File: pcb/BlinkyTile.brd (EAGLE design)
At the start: 49.8 x 47.4 mm, 9 parts

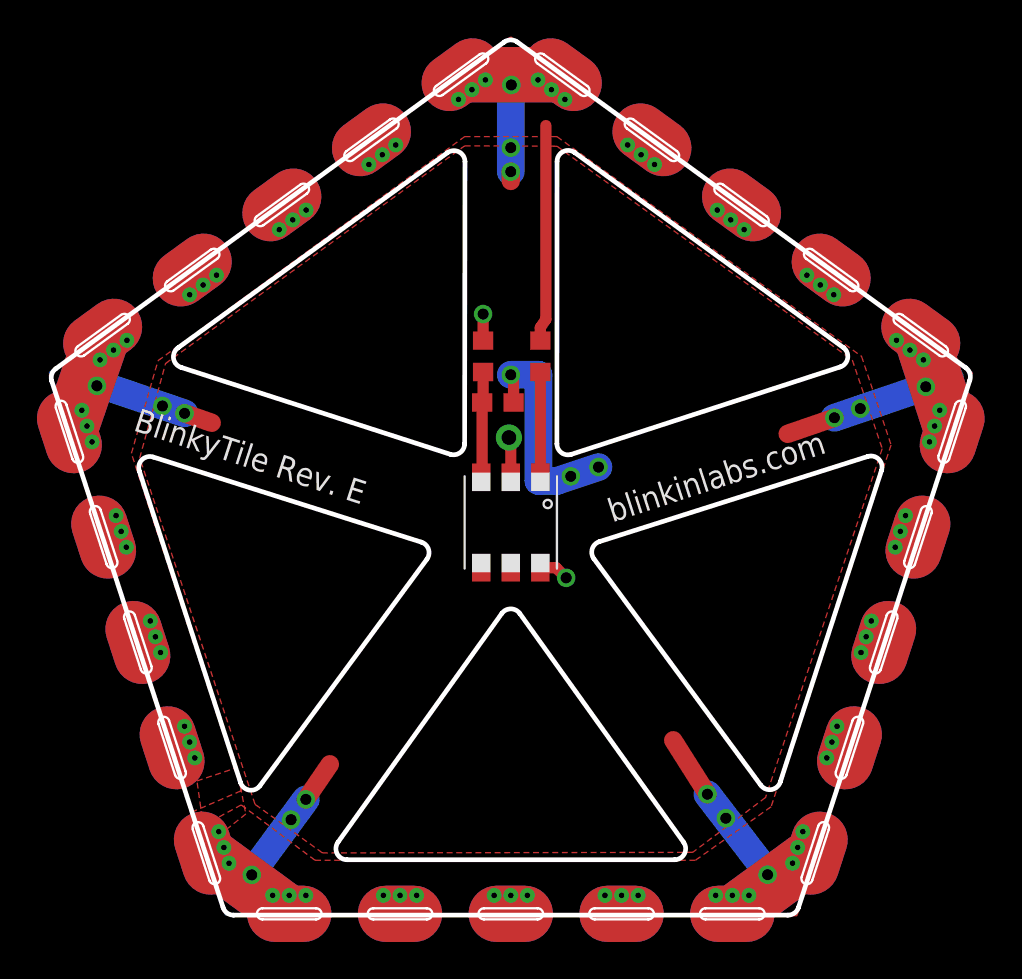
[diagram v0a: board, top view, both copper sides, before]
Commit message: Put address line on edge, tighten R and C positions
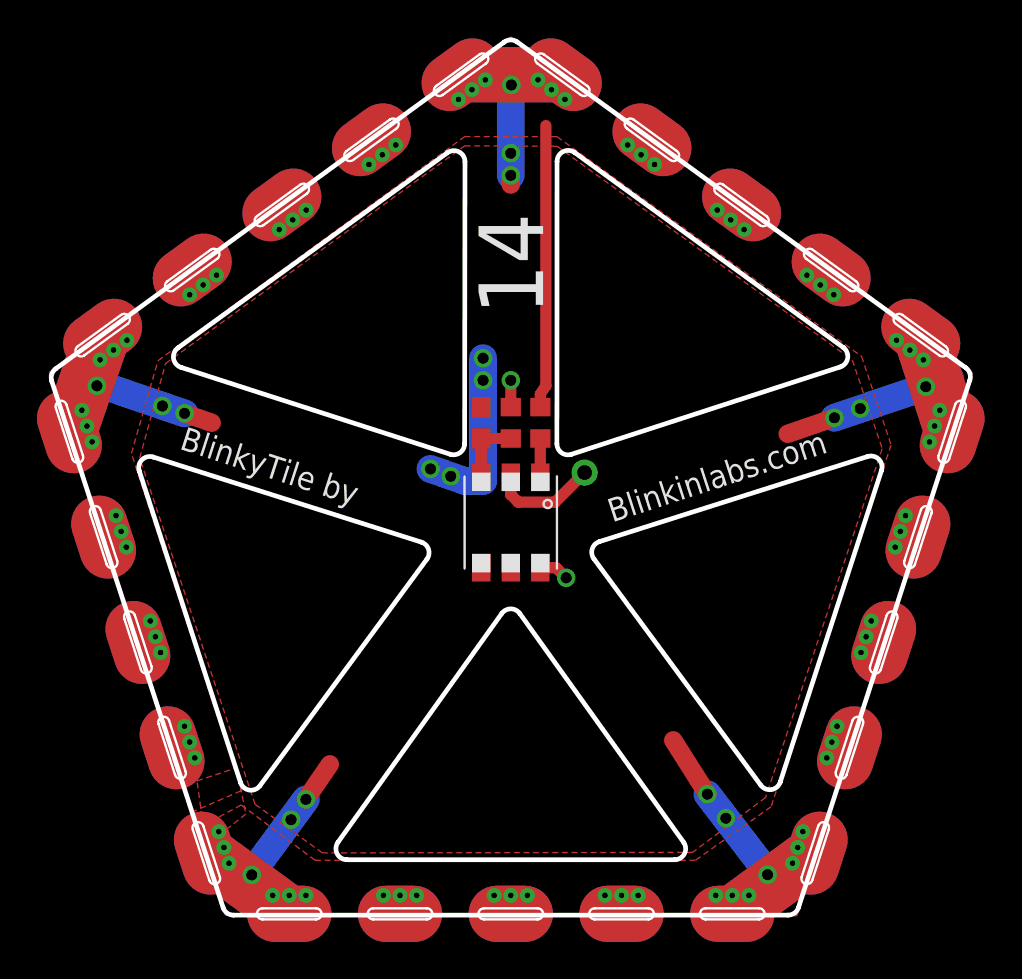
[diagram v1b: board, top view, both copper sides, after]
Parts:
- moved R1 3.90 mm to (0.00, 5.40)
- moved R2 3.60 mm to (1.60, 5.40)
- moved C1 1.42 mm to (-1.60, 5.40), turned to 90 degrees
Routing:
- net N$2: track 5.70 -> 2.10 mm
- net DATA: track 11.7 -> 15.3 mm
- net ADRI: track 2.19 -> 5.78 mm
- net GND: track 123.6 -> 121.2 mm, vias 18 -> 19
- net N$1: track 5.74 -> 3.70 mm
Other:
- board text added: "14"
- board text added: "Blinkinlabs.com"
- board text added: "BlinkyTile by"
- board text removed: "BlinkyTile Rev. E"
- board text removed: "blinkinlabs.com"
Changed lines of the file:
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@@
 <setting verticaltext="up"/>
 </settings>
-<grid distance="1" unitdist="mm" unit="mm" style="lines" multiple="1" display="yes" altdistance="0.5" altunitdist="mm" altunit="mm"/>
+<grid distance="1" unitdist="mm" unit="mm" style="lines" multiple="1" display="yes" altdistance="0.1" altunitdist="mm" altunit="mm"/>
 <layers>
 <layer number="1" name="Top" color="4" fill="1" visible="yes" active="yes"/>
@@
 <layer number="37" name="tTest" color="7" fill="1" visible="no" active="yes"/>
 <layer number="38" name="bTest" color="7" fill="1" visible="no" active="yes"/>
-<layer number="39" name="tKeepout" color="4" fill="11" visible="no" active="yes"/>
+<layer number="39" name="tKeepout" color="4" fill="11" visible="yes" active="yes"/>
 <layer number="40" name="bKeepout" color="1" fill="11" visible="no" active="yes"/>
-<layer number="41" name="tRestrict" color="4" fill="10" visible="no" active="yes"/>
+<layer number="41" name="tRestrict" color="4" fill="10" visible="yes" active="yes"/>
 <layer number="42" name="bRestrict" color="1" fill="10" visible="no" active="yes"/>
 <layer number="43" name="vRestrict" color="2" fill="10" visible="no" active="yes"/>
@@
 <wire x1="8.872346875" y1="-18.27" x2="-8.872346875" y2="-18.27" width="0.254" layer="20"/>
 <wire x1="-8.872346875" y1="-18.27" x2="-9.3601625" y2="-17.320665625" width="0.254" layer="20" curve="-125.607197"/>
-<text x="5.5" y="0" size="1.27" layer="25" rot="R18">blinkinlabs.com</text>
-<text x="-20.5" y="5" size="1.27" layer="25" rot="R342">BlinkyTile Rev. E</text>
+<text x="5.5" y="0" size="1.27" layer="25" rot="R18">Blinkinlabs.com</text>
+<text x="-18" y="4" size="1.27" layer="25" rot="R342">BlinkyTile by</text>
 <wire x1="13.542615625" y1="-14.23260625" x2="4.501234375" y2="-1.965946875" width="0.254" layer="20"/>
 <wire x1="4.501234375" y1="-1.965946875" x2="4.802721875" y2="-1.038065625" width="0.254" layer="20" curve="-108.785562"/>
@@
 <wire x1="3.458484375" y1="20.0384" x2="18.0081875" y2="9.47854375" width="0.254" layer="20"/>
 <wire x1="18.0081875" y1="9.47854375" x2="17.841228125" y2="8.42234375" width="0.254" layer="20" curve="-126.022777"/>
-<polygon width="0.6096" layer="41">
-<vertex x="-2" y="6"/>
-<vertex x="2" y="6"/>
-<vertex x="2" y="4"/>
-<vertex x="2" y="3"/>
-<vertex x="-2" y="3"/>
-</polygon>
+<text x="0" y="14" size="3.5" layer="25" rot="R90" align="center">14</text>
 </plain>
 <attributes>
@@
 </autorouter>
 <elements>
-<element name="C1" library="adafruit" package="C0603" value=".1uF" x="-0.7" y="6.5" smashed="yes"/>
-<element name="R1" library="adafruit" package="R0603" value="75" x="-1.5" y="9" smashed="yes" rot="R270"/>
-<element name="R2" library="adafruit" package="R0603" value="10k" x="1.6" y="9" smashed="yes" rot="R90"/>
+<element name="C1" library="adafruit" package="C0603" value=".1uF" x="-1.6" y="5.4" smashed="yes" rot="R90"/>
+<element name="R1" library="adafruit" package="R0603" value="75" x="0" y="5.4" smashed="yes" rot="R270"/>
+<element name="R2" library="adafruit" package="R0603" value="10k" x="1.6" y="5.4" smashed="yes" rot="R90"/>
 <element name="U$2" library="dodocohedreled" package="D_EDGE_SLOT" value="D_EDGESLOT" x="0" y="-21.2"/>
 <element name="U$3" library="dodocohedreled" package="D_EDGE_SLOT" value="D_EDGESLOT" x="20.2" y="-6.5" rot="R72"/>
@@
 <wire x1="2.45" y1="-2.45" x2="3" y2="-3" width="0.6096" layer="1"/>
 <via x="3" y="-3" extent="1-16" drill="0.6"/>
-<wire x1="-1.5" y1="9.85" x2="-1.5" y2="11.29" width="0.6096" layer="1"/>
-<via x="-1.5" y="11.29" extent="1-16" drill="0.6"/>
+<wire x1="0" y1="6.25" x2="0" y2="7.7" width="0.6096" layer="1"/>
+<via x="0" y="7.7" extent="1-16" drill="0.6"/>
 <contactref element="U$2" pad="PWRVIA1"/>
 <contactref element="U$2" pad="PWRVIA2"/>
@@
 <wire x1="2.79179375" y1="24.253421875" x2="-2.69179375" y2="24.253421875" width="3" layer="16"/>
 <wire x1="-2.69179375" y1="24.253421875" x2="0" y2="24.9" width="1" layer="16"/>
-<wire x1="0" y1="24.9" x2="0" y2="19" width="1.5" layer="16"/>
-<via x="0" y="19" extent="1-16" drill="0.6"/>
-<wire x1="0" y1="19" x2="0" y2="18.5" width="1" layer="1"/>
-<via x="0" y="20.3" extent="1-16" drill="0.6"/>
+<wire x1="0" y1="24.9" x2="0" y2="18.8" width="1.5" layer="16"/>
+<via x="0" y="18.8" extent="1-16" drill="0.6"/>
+<wire x1="0" y1="18.8" x2="0" y2="18.3" width="1" layer="1"/>
+<via x="0" y="20" extent="1-16" drill="0.6"/>
 <wire x1="22.208203125" y1="10.146575" x2="23.8" y2="7.8" width="1" layer="16"/>
 <wire x1="23.8" y1="7.8" x2="17.53" y2="5.67" width="1.5" layer="16"/>
@@
 <via x="13.91" y="-19.08" extent="1-16" drill="0.6"/>
 <contactref element="U$7" pad="4"/>
-<wire x1="0.15" y1="6.5" x2="0.15" y2="7.85" width="0.6096" layer="1"/>
-<wire x1="0.15" y1="7.85" x2="0" y2="8" width="0.6096" layer="1"/>
-<via x="0" y="8" extent="1-16" drill="0.6"/>
-<wire x1="0" y1="8" x2="1.5" y2="8" width="1.5" layer="16"/>
-<wire x1="1.5" y1="8" x2="1.5" y2="2.25" width="1.5" layer="16"/>
-<wire x1="1.5" y1="2.25" x2="2.5" y2="2.25" width="1.5" layer="16"/>
-<wire x1="2.5" y1="2.25" x2="4.75" y2="3" width="1.5" layer="16"/>
-<via x="4.75" y="3" extent="1-16" drill="0.6"/>
-<via x="3.25" y="2.5" extent="1-16" drill="0.6"/>
+<via x="-1.5" y="8.9" extent="1-16" drill="0.6"/>
+<wire x1="-1.5" y1="8.9" x2="-1.5" y2="2.25" width="1.5" layer="16"/>
+<wire x1="-1.5" y1="2.25" x2="-2.5" y2="2.25" width="1.5" layer="16"/>
+<wire x1="-2.5" y1="2.25" x2="-4.35" y2="2.9" width="1.5" layer="16"/>
+<via x="-4.35" y="2.9" extent="1-16" drill="0.6"/>
+<via x="-3.25" y="2.5" extent="1-16" drill="0.6"/>
 <contactref element="U$2" pad="GNDVIA1"/>
 <contactref element="U$2" pad="GNDVIA2"/>
@@
 <contactref element="U$6" pad="GNDVIA5"/>
 <contactref element="U$6" pad="GNDVIA6"/>
+<via x="-1.5" y="7.7" extent="1-16" drill="0.6"/>
 <wire x1="-15.5407375" y1="-17.603659375" x2="-15.262621875" y2="-18.459609375" width="0" layer="19" extent="1-1"/>
 <wire x1="-15.818853125" y1="-16.747709375" x2="-15.5407375" y2="-17.603659375" width="0" layer="19" extent="1-1"/>
@@
 <vertex x="-17" y="-16.6"/>
 </polygon>
-<wire x1="1.6" y1="9.85" x2="1.6" y2="10.55" width="0.6096" layer="1"/>
-<wire x1="1.6" y1="10.55" x2="1.9" y2="11" width="0.6096" layer="1"/>
-<wire x1="1.9" y1="11" x2="1.9" y2="21.5" width="0.6096" layer="1"/>
+<wire x1="1.6" y1="6.25" x2="1.6" y2="6.95" width="0.6096" layer="1"/>
+<wire x1="1.6" y1="6.95" x2="1.9" y2="7.4" width="0.6096" layer="1"/>
+<wire x1="1.9" y1="7.4" x2="1.9" y2="21.5" width="0.6096" layer="1"/>
 <contactref element="U$2" pad="P$8"/>
 <contactref element="U$3" pad="P$8"/>
@@
 <contactref element="C1" pad="1"/>
 <contactref element="R1" pad="2"/>
-<wire x1="-1.55" y1="6.5" x2="-1.55" y2="2.5" width="0.6096" layer="1"/>
-<wire x1="-1.55" y1="2.5" x2="-1.6" y2="2.45" width="0.6096" layer="1"/>
-<wire x1="-1.5" y1="8.15" x2="-1.5" y2="6.55" width="0.6096" layer="1"/>
-<wire x1="-1.5" y1="6.55" x2="-1.55" y2="6.5" width="0.6096" layer="1"/>
+<wire x1="-1.6" y1="4.55" x2="0" y2="4.55" width="0.6096" layer="1"/>
+<wire x1="-1.6" y1="2.45" x2="-1.6" y2="4.55" width="0.6096" layer="1"/>
 </signal>
 <signal name="N$2">
 <contactref element="U$7" pad="1"/>
 <contactref element="R2" pad="1"/>
-<wire x1="1.6" y1="8.15" x2="1.6" y2="2.45" width="0.6096" layer="1"/>
+<wire x1="1.6" y1="4.55" x2="1.6" y2="2.45" width="0.6096" layer="1"/>
 </signal>
 <signal name="ADRI">
-<via x="-0.1" y="4.6" extent="1-16" drill="0.8" diameter="1.4224"/>
+<via x="4" y="2.7" extent="1-16" drill="0.8" diameter="1.4224"/>
 <contactref element="U$7" pad="2"/>
-<wire x1="0" y1="2.45" x2="0" y2="4.5" width="0.6096" layer="1"/>
-<wire x1="0" y1="4.5" x2="-0.1" y2="4.6" width="0.6096" layer="1"/>
+<wire x1="0" y1="2.45" x2="0" y2="1.5" width="0.6096" layer="1"/>
+<wire x1="0" y1="1.5" x2="0.4" y2="1.1" width="0.6096" layer="1"/>
+<wire x1="0.4" y1="1.1" x2="2.4" y2="1.1" width="0.6096" layer="1"/>
+<wire x1="2.4" y1="1.1" x2="4" y2="2.7" width="0.6096" layer="1"/>
 </signal>
 </signals>

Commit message: Bump to RevF: shaped solder masks for different signals
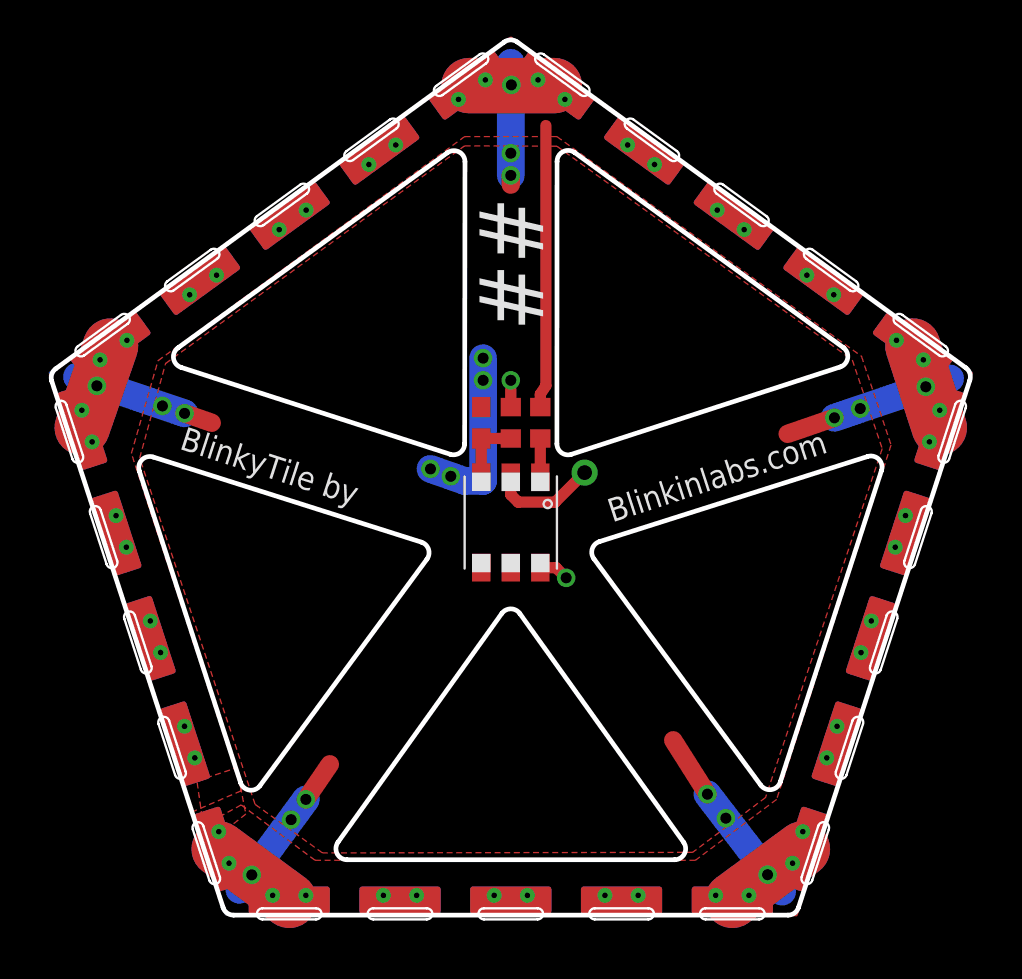
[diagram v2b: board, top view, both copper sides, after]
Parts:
- U$2, U$3, U$4, U$5, U$6: value D_EDGESLOT -> D_EDGEMOD; device dodocohedreled:D_EDGE_SLOT -> dodocohedreled:D_EDGE_SLOT_MOD
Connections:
- net 5V: no longer U$2.PWRVIA2, U$2.PWRVIA5, U$3.PWRVIA2, U$3.PWRVIA5, U$4.PWRVIA2, U$4.PWRVIA5, U$5.PWRVIA2, U$5.PWRVIA5, U$6.PWRVIA2, U$6.PWRVIA5
- net DATA: no longer U$2.SIGVIA2, U$3.SIGVIA2, U$4.SIGVIA2, U$5.SIGVIA2, U$6.SIGVIA2
- net GND: no longer U$2.GNDVIA2, U$2.GNDVIA5, U$3.GNDVIA2, U$3.GNDVIA5, U$4.GNDVIA2, U$4.GNDVIA5, U$5.GNDVIA2, U$5.GNDVIA5, U$6.GNDVIA2, U$6.GNDVIA5
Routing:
- net GND: track 121.2 -> 111.7 mm
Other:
- board text added: "##"
- board text removed: "14"
